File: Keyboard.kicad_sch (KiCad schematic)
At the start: 99 parts, among them SW1 SW_Kailh_1u, SW10 SW_Kailh_1u, SW11 SW_Kailh_1u, SW12 SW_Kailh_1u, SW13 SW_Kailh_1u, SW14 SW_Kailh_1u, SW15 SW_Kailh_1u, SW16 SW_Kailh_1u, SW17 SW_Kailh_1u, SW18 SW_Kailh_1u, SW19 SW_Kailh_1u, SW2 SW_Kailh_1u, SW20 SW_Kailh_1u, SW21 SW_Kailh_1u, SW22 SW_Kailh_1u, SW23 SW_Kailh_1u, SW23_3u1 SW_Kailh_3u, SW24 SW_Kailh_1u, SW25 SW_Kailh_1u, SW26 SW_Kailh_1u, SW27 SW_Kailh_1u, SW28 SW_Kailh_1u, SW29 SW_Kailh_1u, SW3 SW_Kailh_1u, SW30 SW_Kailh_1u, SW31 SW_Kailh_1u, SW32 SW_Kailh_1u, SW33 SW_Kailh_1u, SW34 SW_Kailh_1u, SW35 SW_Kailh_1u, SW36 SW_Kailh_1u, SW37 SW_Kailh_1u, SW38 SW_Kailh_1u, SW39 SW_Kailh_1u, SW4 SW_Kailh_1u, SW40 SW_Kailh_1u, SW41 SW_Kailh_1u, SW42 SW_Kailh_1u, SW43 SW_Kailh_1u, SW44 SW_Kailh_1u, SW45 SW_Kailh_1u, SW5 SW_Kailh_1u, SW6 SW_Kailh_1u, SW7 SW_Kailh_1u, SW8 SW_Kailh_1u, SW9 SW_Kailh_1u, U1 PCAL6416APW, U2 Seeed Studio XIAO SAMD21

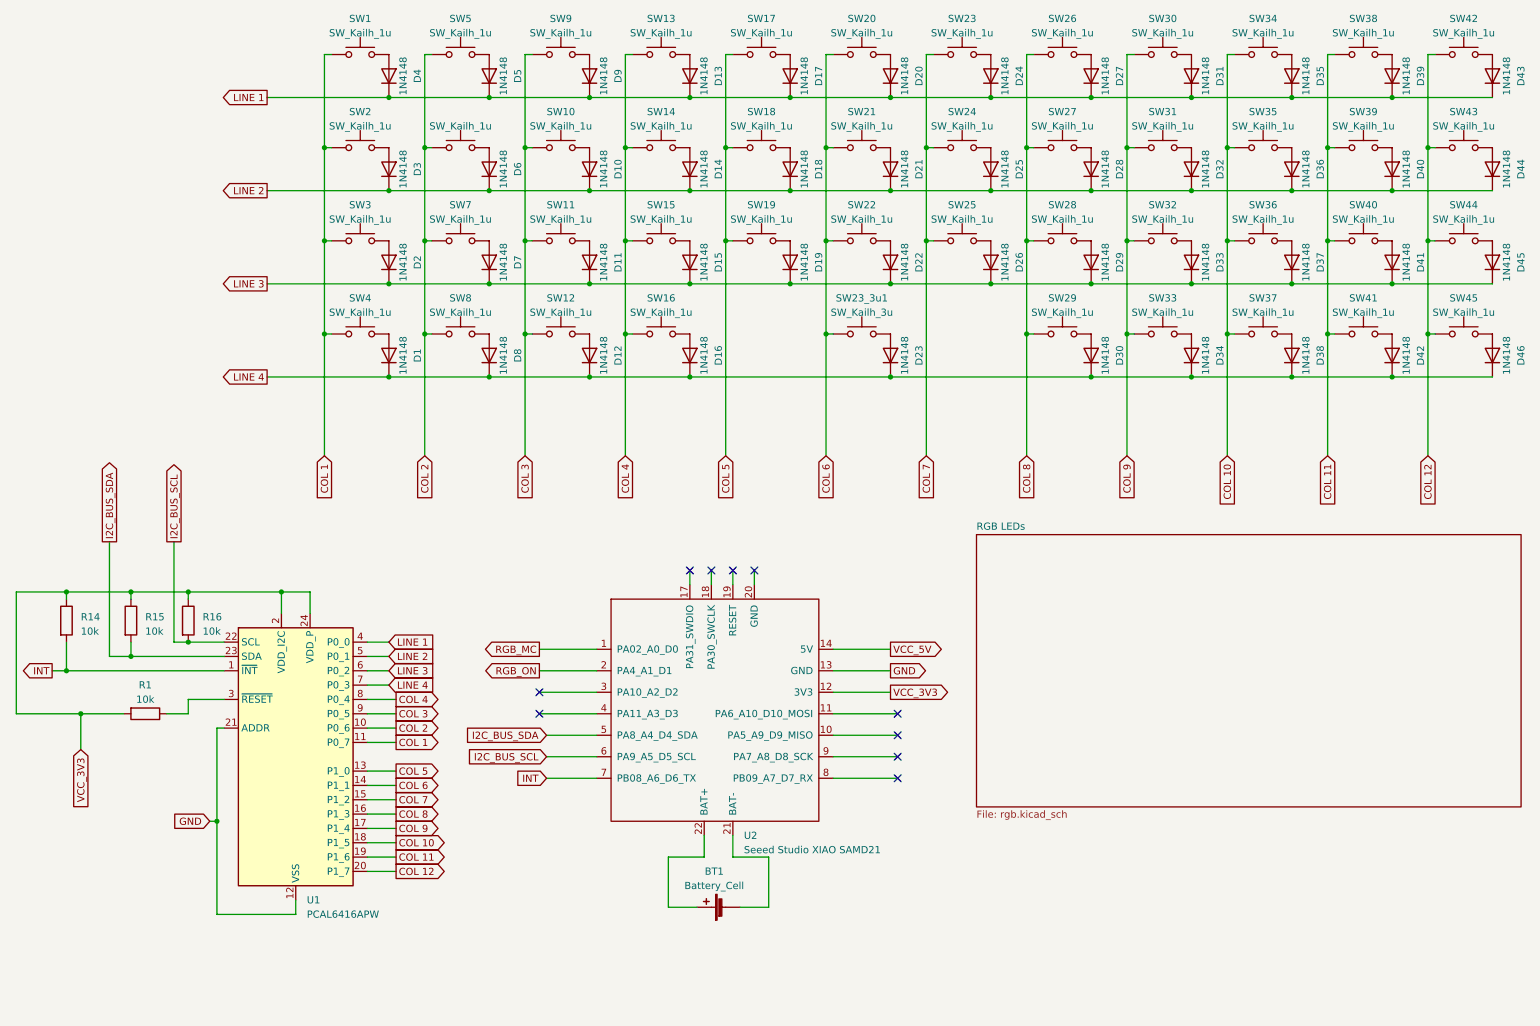
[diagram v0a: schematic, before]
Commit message: finished pcb routing
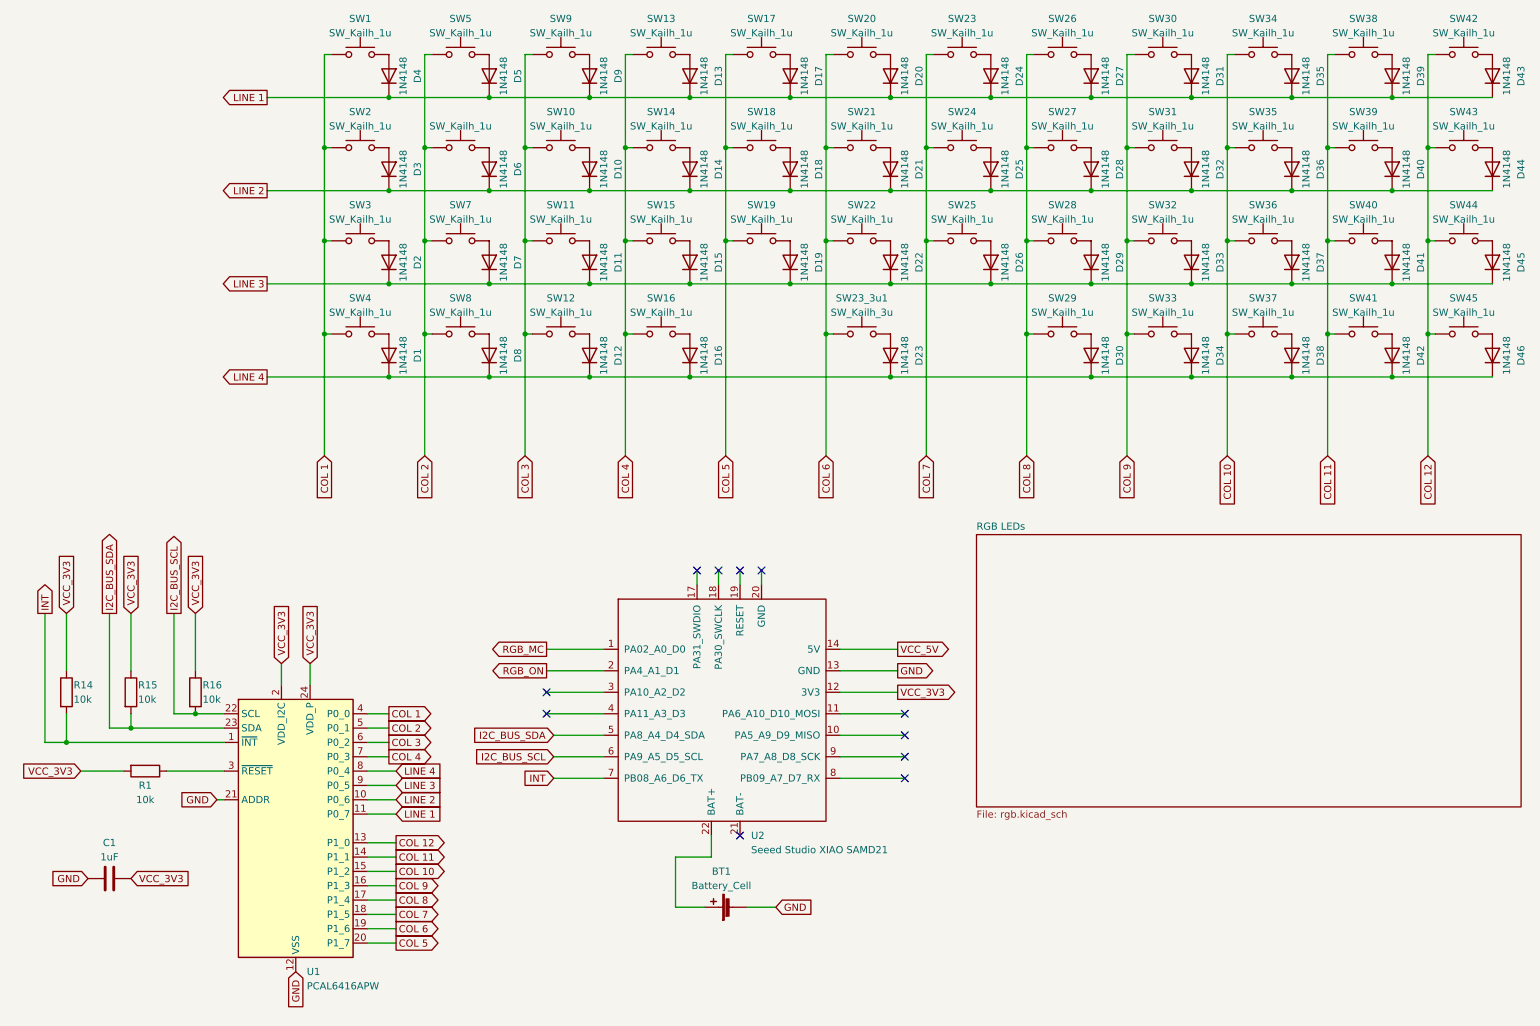
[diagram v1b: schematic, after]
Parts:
- added C1: 1uF, Capacitor_SMD:C_0805_2012Metric_Pad1.18x1.45mm_HandSolder, symbol Device:C
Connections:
- net COL 1: now also U1.4 (P0_0); no longer U1.11 (P0_7)
- net COL 10: now also U1.15 (P1_2); no longer U1.18 (P1_5)
- net COL 11: now also U1.14 (P1_1); no longer U1.19 (P1_6)
- net COL 12: now also U1.13 (P1_0); no longer U1.20 (P1_7)
- net COL 2: now also U1.5 (P0_1); no longer U1.10 (P0_6)
- net COL 3: now also U1.6 (P0_2); no longer U1.9 (P0_5)
- net COL 4: now also U1.7 (P0_3); no longer U1.8 (P0_4)
- net COL 5: now also U1.20 (P1_7); no longer U1.13 (P1_0)
- net COL 6: now also U1.19 (P1_6); no longer U1.14 (P1_1)
- net COL 7: now also U1.18 (P1_5); no longer U1.15 (P1_2)
- net COL 8: now also U1.17 (P1_4); no longer U1.16 (P1_3)
- net COL 9: now also U1.16 (P1_3); no longer U1.17 (P1_4)
- net GND: now also BT1.2 (-), C1.2
- net LINE 1: now also U1.11 (P0_7); no longer U1.4 (P0_0)
- net LINE 2: now also U1.10 (P0_6); no longer U1.5 (P0_1)
- net LINE 3: now also U1.9 (P0_5); no longer U1.6 (P0_2)
- net LINE 4: now also U1.8 (P0_4); no longer U1.7 (P0_3)
- net VCC_3V3: now also C1.1
- net at U2.21 (BAT-): no longer BT1.2 (-)
- no-connect marks 10 -> 11
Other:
- moved on the sheet: BT1, R1, R14, R15, R16, U1, U2

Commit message: rev 1.2
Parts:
- D1, D10, D11, D12, D13, D14, D15, D16, D17, D18, D19, D2, D20, D21, D22, D23, D24, D25, D26, D27, D28, D29, D3, D30, D31, D32, D33, D34, D35, D36, D37, D38, D39, D4, D40, D41, D42, D43, D44, D45, D46, D5, D6, D7, D8, D9: value 1N4148 -> 1N4148W; footprint Diode_SMD:D_1206_3216Metric_Pad1.42x1.75mm_HandSolder -> Diode_SMD:D_SOD-123
